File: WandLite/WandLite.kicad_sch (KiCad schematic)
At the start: 17 parts, among them J4 Conn_01x03_Pin, J9 Conn_01x02_Pin, SW1 SW_SPDT_312, SW2 SW_SPDT_312, U1 ATtiny85-20P

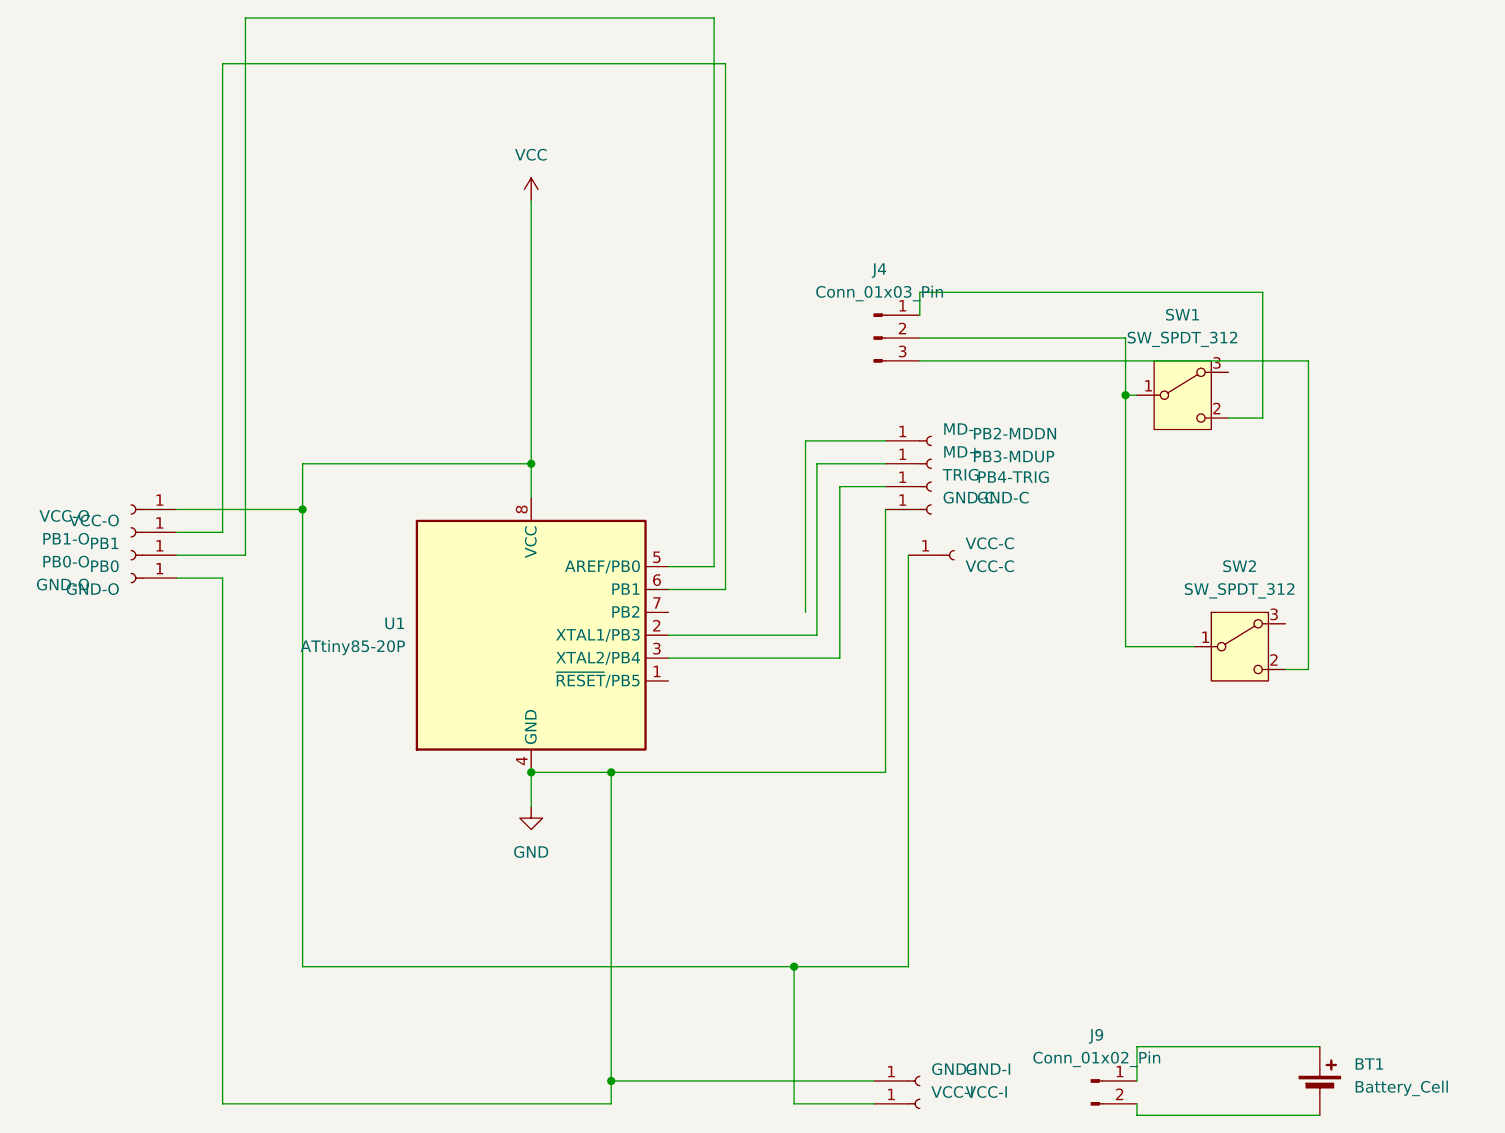
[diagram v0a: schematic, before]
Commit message: removed mode- for vcc-c
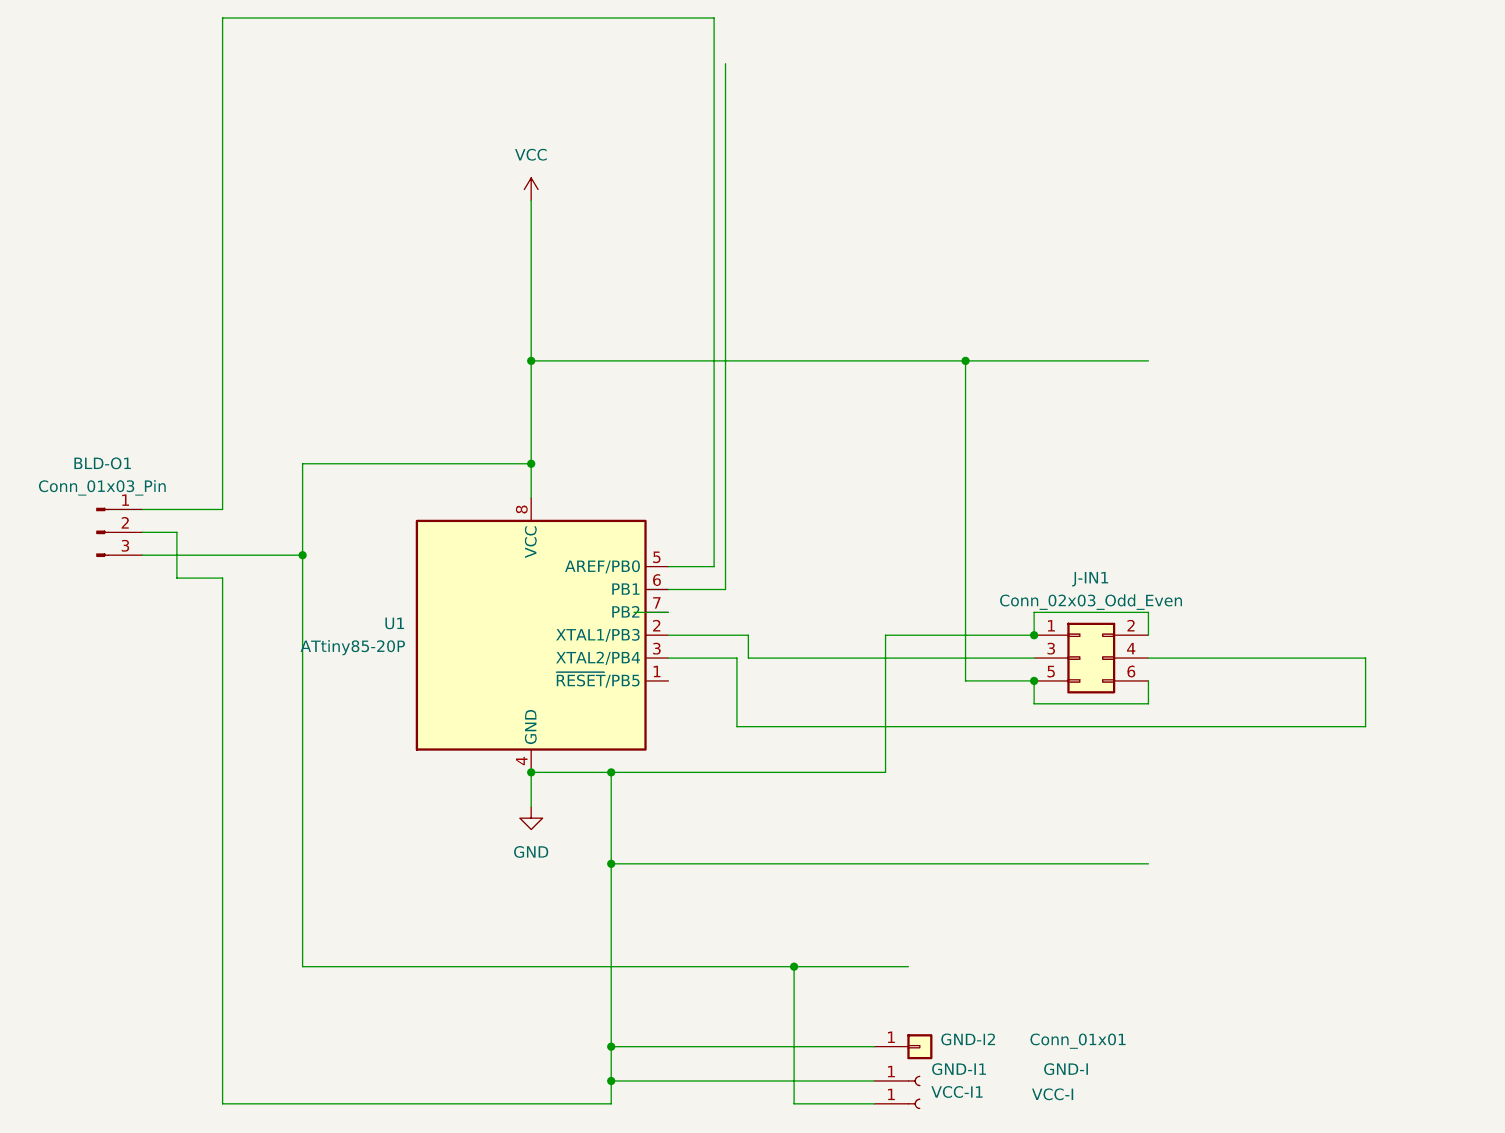
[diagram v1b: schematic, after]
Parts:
- removed BT1: Battery_Cell, symbol Device:Battery_Cell
- removed GND-C: GND-C, Kelvin_Library:SolderWire-0.15sqmm_1x01_D0.5mm_OD1.5mm_Relief_SHORT, symbol Connector:Conn_01x01_Socket
- removed GND-O: GND-O, Kelvin_Library:SolderWire-0.15sqmm_1x01_D0.5mm_OD1.5mm_Relief_SHORT, symbol Connector:Conn_01x01_Socket
- removed J4: Conn_01x03_Pin, symbol Connector:Conn_01x03_Pin
- removed J9: Conn_01x02_Pin, symbol Connector:Conn_01x02_Pin
- removed MD+: PB3-MDUP, Kelvin_Library:SolderWire-0.15sqmm_1x01_D0.5mm_OD1.5mm_Relief_SHORT, symbol Connector:Conn_01x01_Socket
- removed MD-: PB2-MDDN, Kelvin_Library:SolderWire-0.15sqmm_1x01_D0.5mm_OD1.5mm_Relief_SHORT, symbol Connector:Conn_01x01_Socket
- removed PB0: PB0-O, Kelvin_Library:SolderWire-0.15sqmm_1x01_D0.5mm_OD1.5mm_Relief_SHORT, symbol Connector:Conn_01x01_Socket
- removed PB1: PB1-O, Kelvin_Library:SolderWire-0.15sqmm_1x01_D0.5mm_OD1.5mm_Relief_SHORT, symbol Connector:Conn_01x01_Socket
- removed SW1, SW2: SW_SPDT_312, symbol Switch:SW_SPDT_312
- removed TRIG: PB4-TRIG, Kelvin_Library:SolderWire-0.15sqmm_1x01_D0.5mm_OD1.5mm_Relief_SHORT, symbol Connector:Conn_01x01_Socket
- removed VCC-C: VCC-C, Kelvin_Library:SolderWire-0.15sqmm_1x01_D0.5mm_OD1.5mm_Relief_SHORT, symbol Connector:Conn_01x01_Socket
- removed VCC-O: VCC-O, Kelvin_Library:SolderWire-0.15sqmm_1x01_D0.5mm_OD1.5mm_Relief_SHORT, symbol Connector:Conn_01x01_Socket
- added BLD-O1: Conn_01x03_Pin, Connector_JST:JST_PH_S3B-PH-K_1x03_P2.00mm_Horizontal, symbol Connector:Conn_01x03_Pin
- added GND-I2: Conn_01x01, Connector_Wire:SolderWire-0.15sqmm_1x01_D0.5mm_OD1.5mm, symbol Connector_Generic:Conn_01x01
- added J-IN1: Conn_02x03_Odd_Even, Connector_PinHeader_2.54mm:PinHeader_2x03_P2.54mm_Vertical, symbol Connector_Generic:Conn_02x03_Odd_Even
- GND-I1: renamed from GND-I; footprint Kelvin_Library:SolderWire-0.15sqmm_1x01_D0.5mm_OD1.5mm_Relief_SHORT -> Connector_Wire:SolderWire-0.15sqmm_1x01_D0.5mm_OD1.5mm
- VCC-I1: renamed from VCC-I; footprint Kelvin_Library:SolderWire-0.15sqmm_1x01_D0.5mm_OD1.5mm_Relief_SHORT -> Connector_Wire:SolderWire-0.15sqmm_1x01_D0.5mm_OD1.5mm
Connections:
- net GND: now also BLD-O1.2 (Pin_2), GND-I2.1 (Pin_1), J-IN1.1 (Pin_1), J-IN1.2 (Pin_2)
- net VCC: now also BLD-O1.3 (Pin_3), J-IN1.5 (Pin_5), J-IN1.6 (Pin_6)
- net at U1.2 (XTAL1/PB3): now also J-IN1.3 (Pin_3)
- net at U1.5 (AREF/PB0): now also BLD-O1.1 (Pin_1)
- net at U1.3 (XTAL2/PB4): now also J-IN1.4 (Pin_4)

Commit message: v5 made vertical
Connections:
- net at J-IN1.3 (Pin_3): now also U1.3 (XTAL2/PB4); no longer U1.2 (XTAL1/PB3)
- net at J-IN1.4 (Pin_4): now also U1.2 (XTAL1/PB3); no longer U1.3 (XTAL2/PB4)
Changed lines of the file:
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@@
-	(wire
-		(pts
-			(xy 201.93 109.22) (xy 170.18 109.22)
-		)
-		(stroke
-			(width 0)
-			(type default)
-		)
-	)
 	(wire
 		(pts
@@
 	(wire
 		(pts
+			(xy 201.93 109.22) (xy 198.12 109.22)
+		)
+		(stroke
+			(width 0)
+			(type default)
+		)
+	)
+	(wire
+		(pts
 			(xy 201.93 104.14) (xy 201.93 106.68)
 		)
@@
 	(wire
 		(pts
+			(xy 190.5 109.22) (xy 190.5 116.84)
+		)
+		(stroke
+			(width 0)
+			(type default)
+		)
+	)
+	(wire
+		(pts
 			(xy 111.76 158.75) (xy 154.94 158.75)
 		)
@@
 	(wire
 		(pts
+			(xy 170.18 109.22) (xy 190.5 109.22)
+		)
+		(stroke
+			(width 0)
+			(type default)
+		)
+	)
+	(wire
+		(pts
 			(xy 175.26 158.75) (xy 175.26 143.51)
 		)
@@
 	(wire
 		(pts
+			(xy 198.12 119.38) (xy 168.91 119.38)
+		)
+		(stroke
+			(width 0)
+			(type default)
+		)
+	)
+	(wire
+		(pts
 			(xy 201.93 111.76) (xy 194.31 111.76)
 		)
@@
 	(wire
 		(pts
-			(xy 168.91 116.84) (xy 238.76 116.84)
-		)
-		(stroke
-			(width 0)
-			(type default)
-		)
-	)
-	(wire
-		(pts
 			(xy 185.42 106.68) (xy 201.93 106.68)
 		)
@@
 	(wire
 		(pts
+			(xy 198.12 109.22) (xy 198.12 119.38)
+		)
+		(stroke
+			(width 0)
+			(type default)
+		)
+	)
+	(wire
+		(pts
 			(xy 194.31 111.76) (xy 194.31 76.2)
 		)
@@
 	(wire
 		(pts
+			(xy 190.5 116.84) (xy 238.76 116.84)
+		)
+		(stroke
+			(width 0)
+			(type default)
+		)
+	)
+	(wire
+		(pts
 			(xy 146.05 58.42) (xy 146.05 76.2)
 		)
@@
 	(wire
 		(pts
-			(xy 168.91 109.22) (xy 168.91 116.84)
-		)
-		(stroke
+			(xy 168.91 109.22) (xy 168.91 119.38)
+		)
+		(stroke
